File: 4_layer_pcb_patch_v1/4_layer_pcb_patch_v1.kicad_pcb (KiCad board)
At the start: 4 copper layers, 131 x 131 mm, 1 part, among them J1 Conn_Coaxial_Small

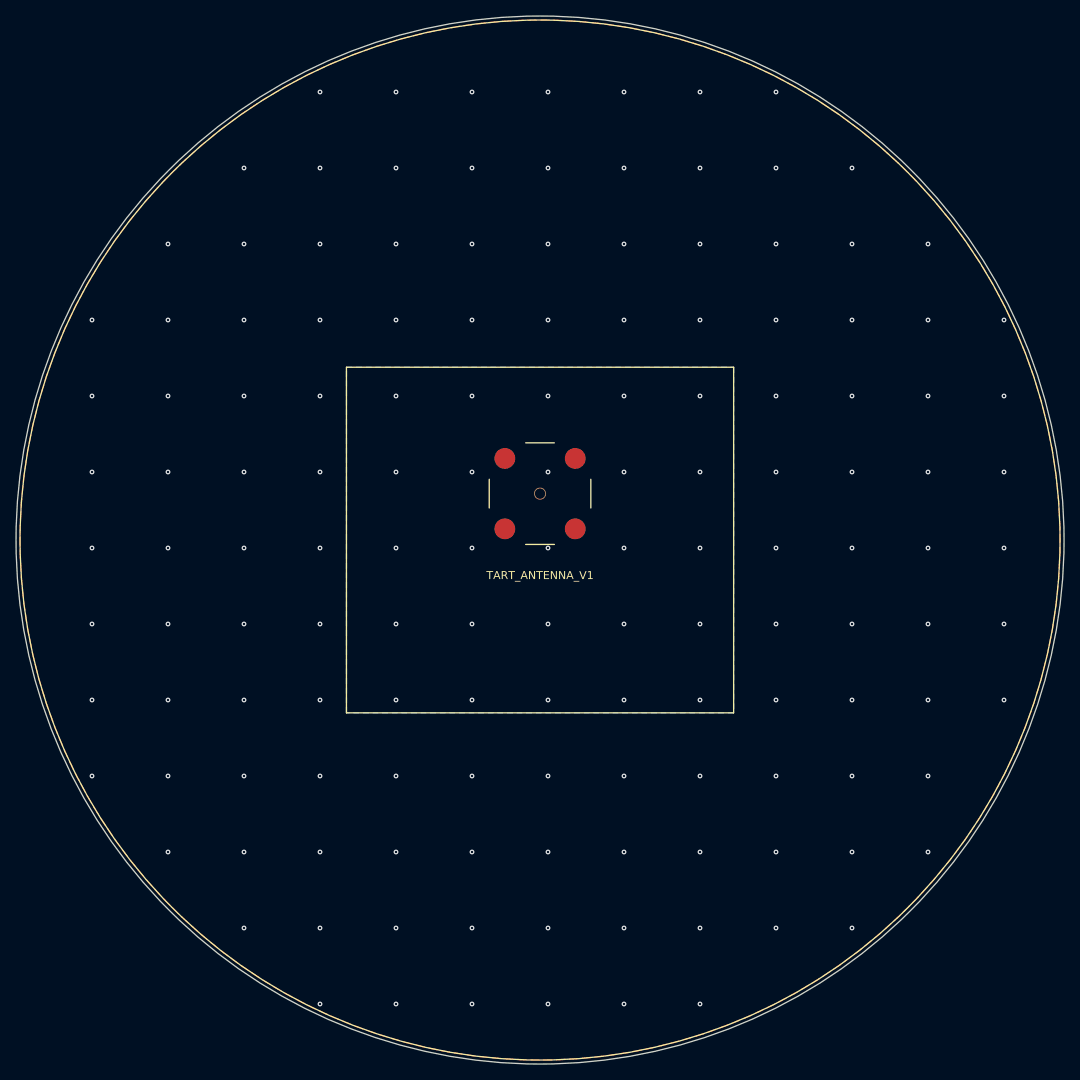
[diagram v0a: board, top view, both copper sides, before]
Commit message: Ground vias adjusted
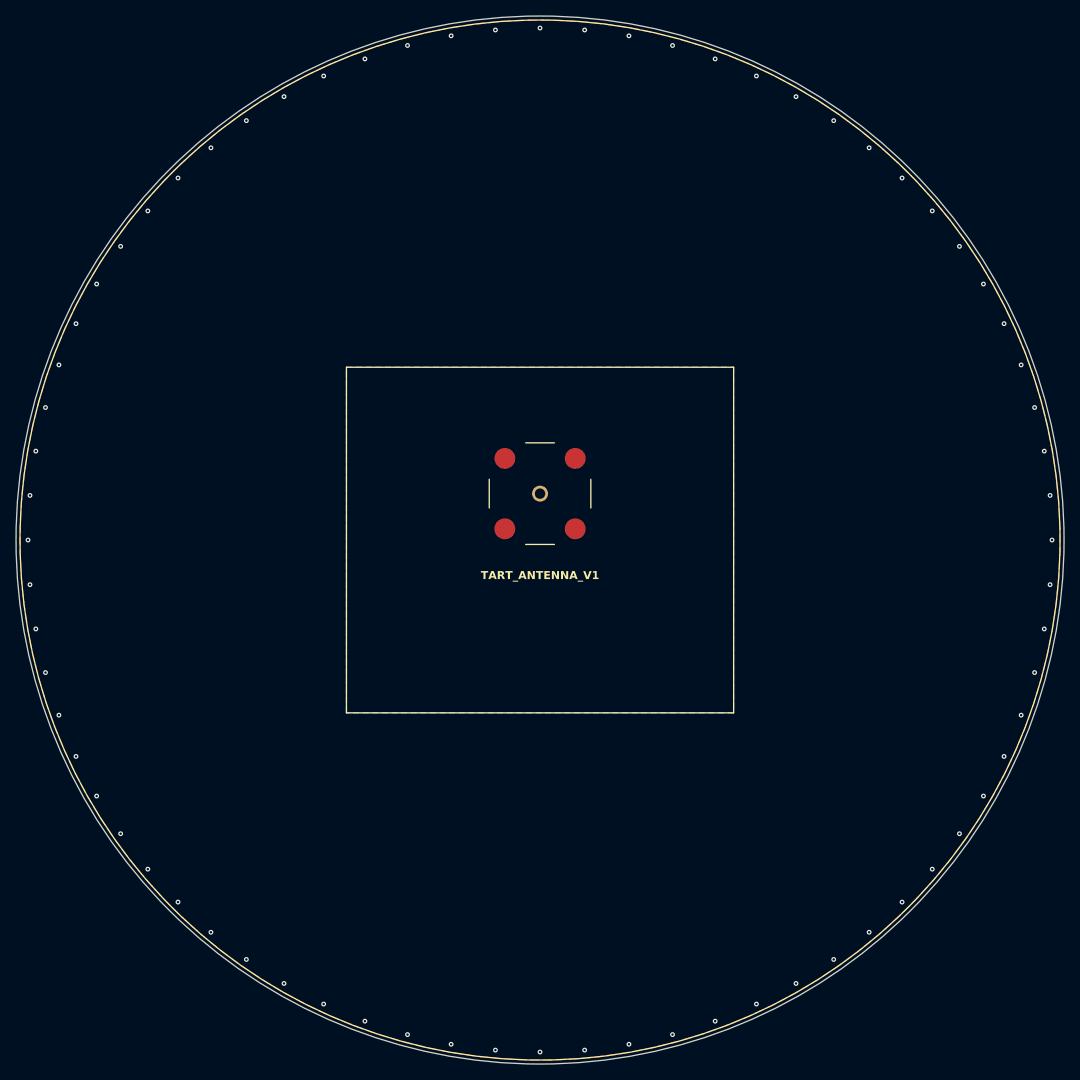
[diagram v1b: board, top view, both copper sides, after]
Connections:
- J1 pad 1: unconnected-(J1-In-Pad1) -> /patch_element
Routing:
- net GND: vias 143 -> 72
- added copper zone on B.Cu, net /patch_element
- removed copper zone on B.Cu, net unconnected-(J1-In-Pad1)
